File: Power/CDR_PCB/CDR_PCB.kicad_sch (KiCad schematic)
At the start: 69 parts, among them IC1 TEENSY_4.1, J1 L2596S-3.3-Breakout, J10 Transceiver header, J2 MT3608-Breakout, J3 Lower_PCB_Header, J4 LM2596S-5-Breakout, J5 +14Vin, J6 +14Vout, J7 MOTOR2, J8 MOTOR1, J9 Converter_GND_Lines, U1 INA226, U2 BNO055, U3 DPS310XTSA1, U4 GNSS, U5 DRV8871, U6 MICROFC-30035-SMT-TR1, U7 HTS221, U8 OPA333xxD, U9 OPA333xxD

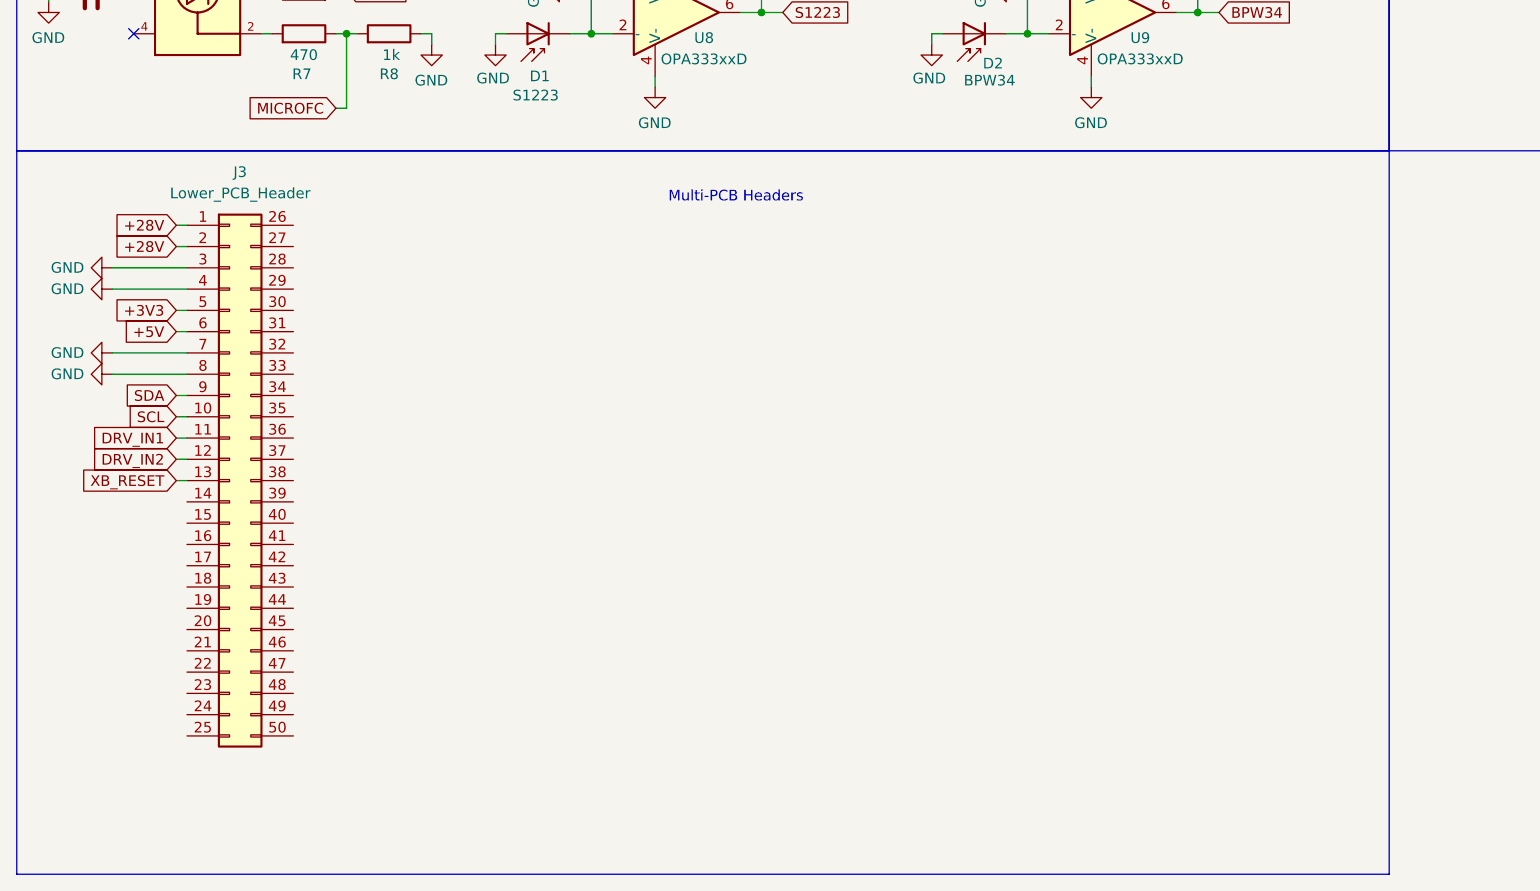
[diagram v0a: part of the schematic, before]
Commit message: Moved final PCB designs to seperate kicad project
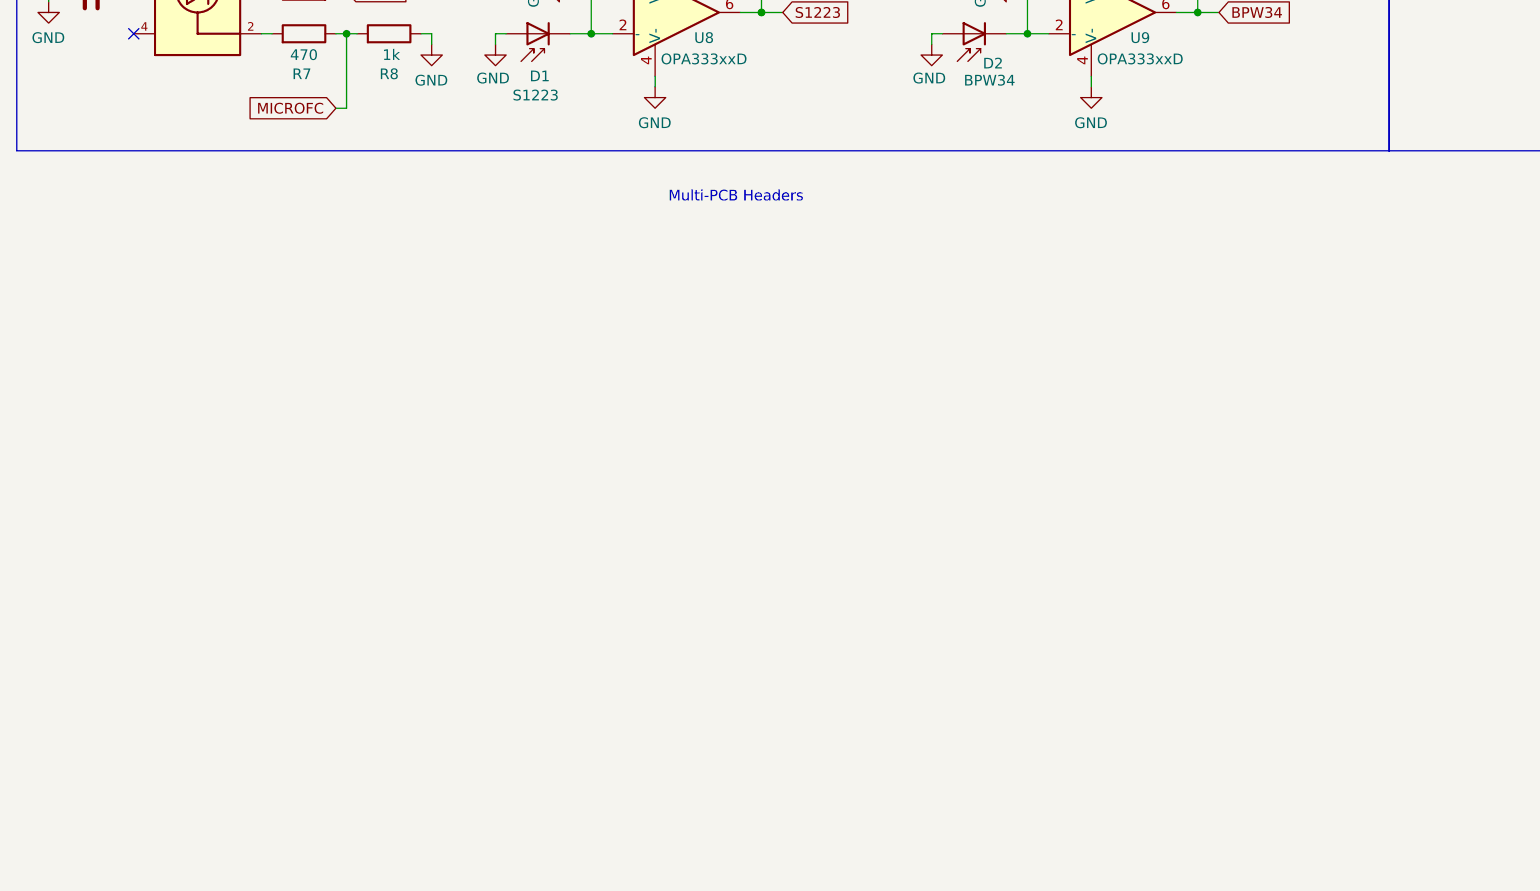
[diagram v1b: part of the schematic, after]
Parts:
- removed J3: Lower_PCB_Header, symbol Connector_Generic:Conn_02x25_Top_Bottom
- U3: DESCRIPTION Supply voltage range 1.7V to 3.6V | Operation range 300hPa 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 -> (none)

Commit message: commit before temp rollback for dimension checks
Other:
- note removed: "Multi-PCB Headers"
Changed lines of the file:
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@@
-		)
-	)
-	(text "Multi-PCB Headers\n"
-		(exclude_from_sim no)
-		(at 98.552 202.438 0)
-		(effects
-			(font
-				(size 1.27 1.27)
-			)
 		)
 	)
